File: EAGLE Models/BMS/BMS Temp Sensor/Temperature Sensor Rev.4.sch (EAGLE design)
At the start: 7 parts

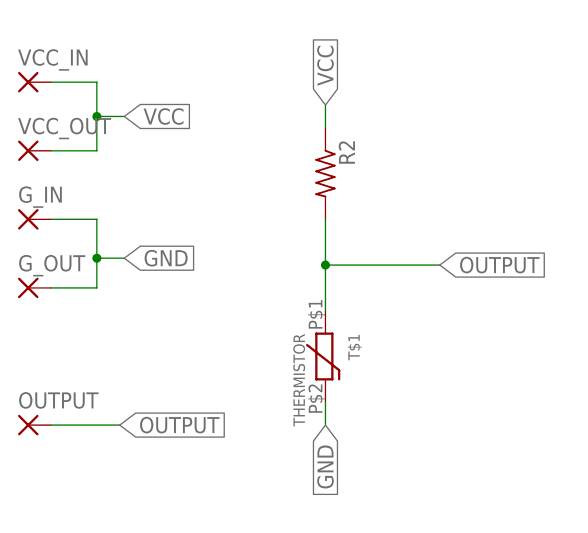
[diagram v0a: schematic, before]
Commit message: Set Resistance Values for the Temp Sense Board and Fixed ADC Connections
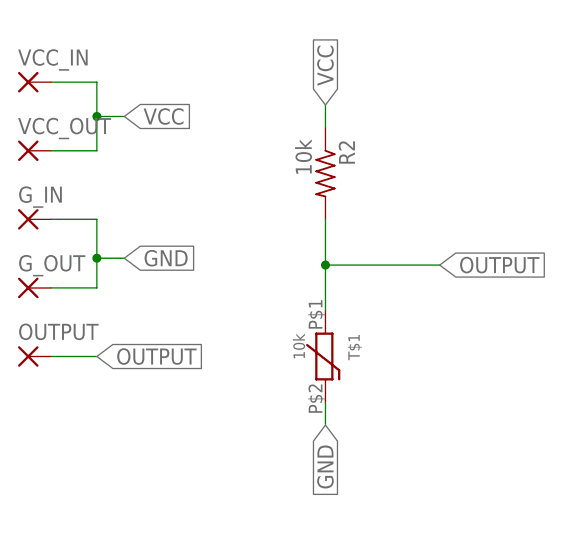
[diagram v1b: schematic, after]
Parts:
- R2: value (none) -> 10k
- T$1: value THERMISTOR -> 10k
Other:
- moved on the sheet: OUTPUT
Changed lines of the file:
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@@
 <part name="OUTPUT" library="wirepad" deviceset="1,6/0,8" device=""/>
 <part name="G_OUT" library="wirepad" deviceset="1,6/0,8" device=""/>
-<part name="T$1" library="formula electric" deviceset="THERMISTOR" device=""/>
-<part name="R2" library="resistor" deviceset="R-US_" device="R0603"/>
+<part name="T$1" library="formula electric" deviceset="THERMISTOR" device="" value="10k"/>
+<part name="R2" library="resistor" deviceset="R-US_" device="R0603" value="10k"/>
 </parts>
 <sheets>
@@
 <instance part="G_IN" gate="P" x="40.64" y="60.96"/>
 <instance part="VCC_OUT" gate="P" x="40.64" y="68.58"/>
-<instance part="OUTPUT" gate="P" x="40.64" y="38.1"/>
+<instance part="OUTPUT" gate="P" x="40.64" y="45.72"/>
 <instance part="G_OUT" gate="P" x="40.64" y="53.34"/>
 <instance part="T$1" gate="T$1" x="73.66" y="45.72" rot="R270"/>
@@
 <segment>
 <pinref part="OUTPUT" gate="P" pin="P"/>
-<wire x1="43.18" y1="38.1" x2="50.8" y2="38.1" width="0.1524" layer="91"/>
-<label x="50.8" y="38.1" size="1.778" layer="95" xref="yes"/>
+<wire x1="43.18" y1="45.72" x2="48.26" y2="45.72" width="0.1524" layer="91"/>
+<label x="48.26" y="45.72" size="1.778" layer="95" xref="yes"/>
 </segment>
 <segment>

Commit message: Temp Sense Board Layouts Finished First revision, bunch of test layouts to get estimate of board sizes
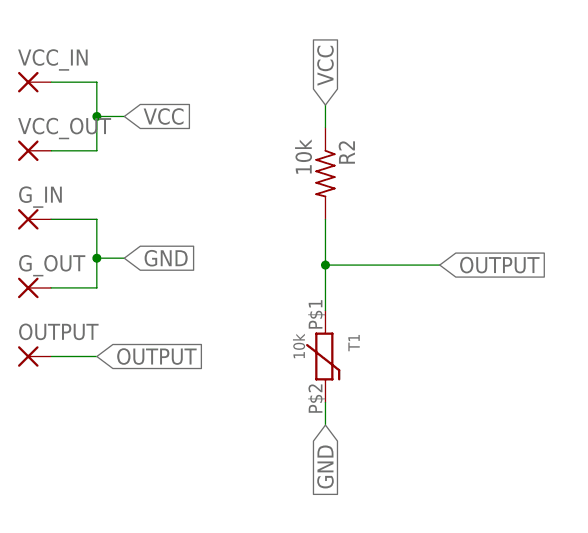
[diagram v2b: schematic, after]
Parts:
- renumbered T$1 to T1
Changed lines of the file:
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@@
 <part name="OUTPUT" library="wirepad" deviceset="1,6/0,8" device=""/>
 <part name="G_OUT" library="wirepad" deviceset="1,6/0,8" device=""/>
-<part name="T$1" library="formula electric" deviceset="THERMISTOR" device="" value="10k"/>
+<part name="T1" library="formula electric" deviceset="THERMISTOR" device="" value="10k"/>
 <part name="R2" library="resistor" deviceset="R-US_" device="R0603" value="10k"/>
 </parts>
@@
 <instance part="OUTPUT" gate="P" x="40.64" y="45.72"/>
 <instance part="G_OUT" gate="P" x="40.64" y="53.34"/>
-<instance part="T$1" gate="T$1" x="73.66" y="45.72" rot="R270"/>
+<instance part="T1" gate="T$1" x="73.66" y="45.72" rot="R270"/>
 <instance part="R2" gate="G$1" x="73.66" y="66.04" rot="R270"/>
 </instances>
@@
 <wire x1="73.66" y1="40.64" x2="73.66" y2="38.1" width="0.1524" layer="91"/>
 <label x="73.66" y="38.1" size="1.778" layer="95" rot="R270" xref="yes"/>
-<pinref part="T$1" gate="T$1" pin="P$2"/>
+<pinref part="T1" gate="T$1" pin="P$2"/>
 </segment>
 <segment>
@@
 <wire x1="73.66" y1="55.88" x2="73.66" y2="60.96" width="0.1524" layer="91"/>
 <junction x="73.66" y="55.88"/>
-<pinref part="T$1" gate="T$1" pin="P$1"/>
+<pinref part="T1" gate="T$1" pin="P$1"/>
 <pinref part="R2" gate="G$1" pin="2"/>
 <label x="86.36" y="55.88" size="1.778" layer="95" xref="yes"/>
